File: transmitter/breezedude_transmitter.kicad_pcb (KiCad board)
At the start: 2 copper layers, 53 x 22.5 mm, 53 parts, among them J1 Conn_01x02_Pin, J11 Conn_01x04_Pin, J2 Conn_01x04_Pin, J3 Conn_01x04_Pin, J4 Conn_01x03_Pin, J5 Conn_01x04_Pin, J6 Conn_01x02_Pin, J7 USB_C_Receptacle_USB2.0_16P, Q2 P-MOS, Q3 P-MOS, SW1 SW_Push, U1 D1213A-04TS-7, U10 D1213A-04TS-7, U2 STLQ015M33R, U3 ATSAMD21G18A-A, U8 HP203B, U9 TP4057

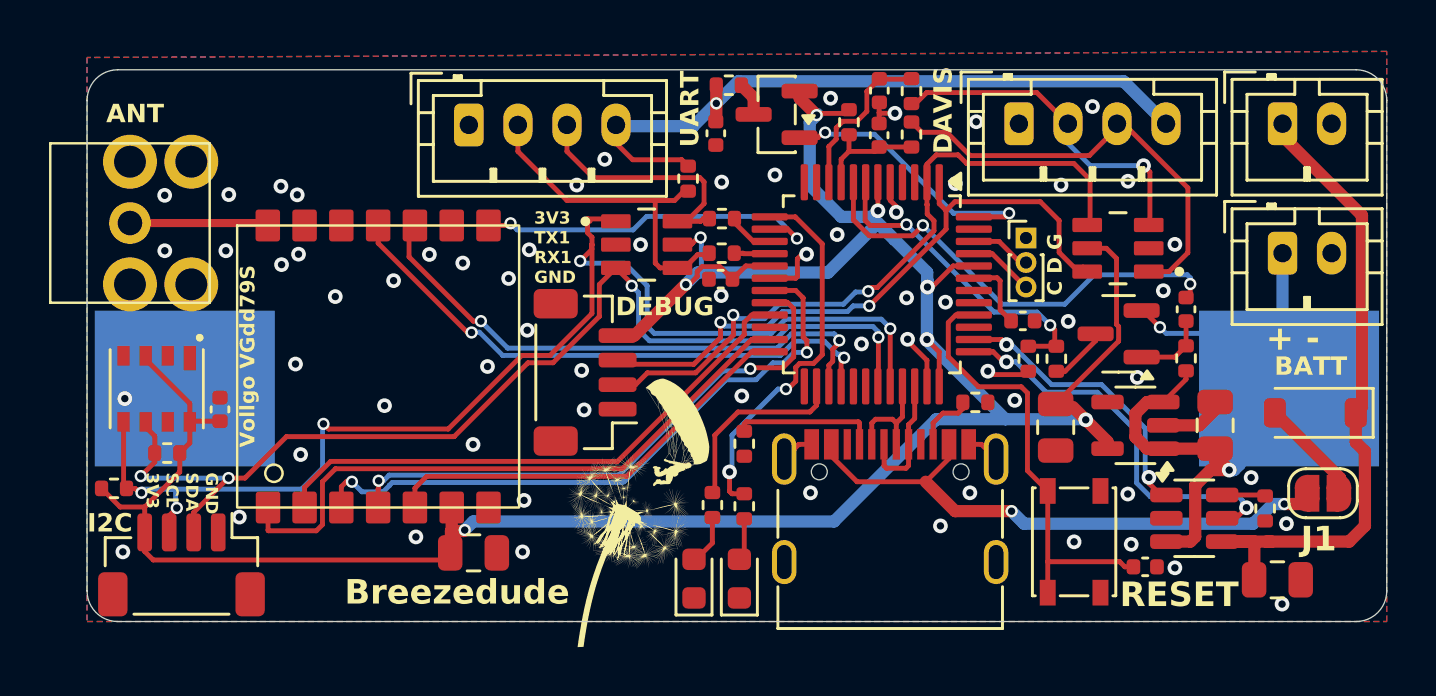
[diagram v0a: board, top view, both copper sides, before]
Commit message: V2.5 - some pin changes and improvements. Requires FW 1.2.0+
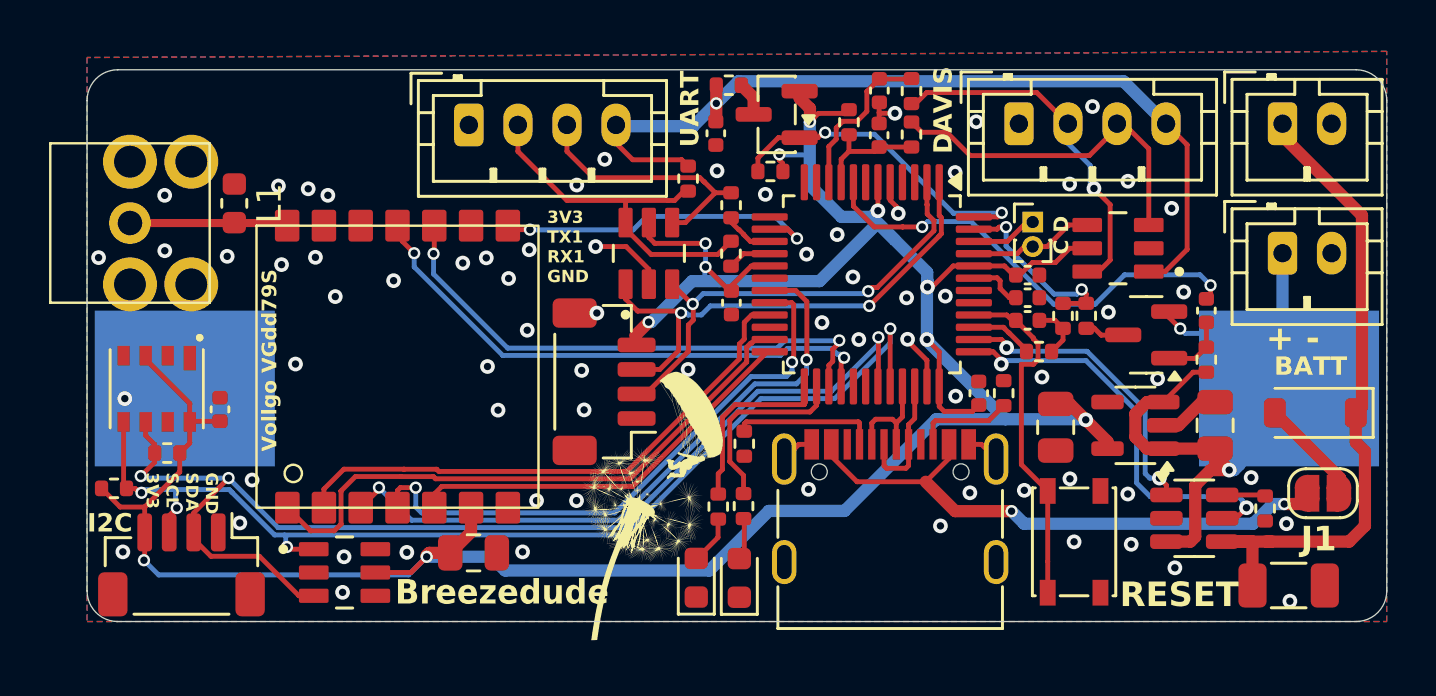
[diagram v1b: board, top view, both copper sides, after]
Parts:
- removed J4: Conn_01x03_Pin, Connector_PinHeader_1.00mm:PinHeader_1x03_P1.00mm_Vertical
- added C10: 100n 16V, Capacitor_SMD:C_0402_1005Metric, F.Cu at (133.4, 114.7)
- added C14: 100n 16V, Capacitor_SMD:C_0402_1005Metric, F.Cu at (135.4, 109.9)
- added J8: Conn_01x02_Pin, Connector_PinHeader_1.00mm:PinHeader_1x02_P1.00mm_Vertical, F.Cu at (135.6, 107.7)
- added L1: 68nH, Inductor_SMD:L_0603_1608Metric, F.Cu at (103.0, 106.9)
- added R18: 1M5, Resistor_SMD:R_0402_1005Metric, F.Cu at (124.9, 105.6)
- added R19: 4k7, Resistor_SMD:R_0402_1005Metric, F.Cu at (135.8, 113.0)
- added U11: D1213A-04TS-7, footprints:SOT95P280X140-6N, F.Cu at (119.9, 109.0)
- C1: value 47u 6.3V -> 47u 10V; footprint Capacitor_SMD:C_0805_2012Metric -> Capacitor_SMD:C_1206_3216Metric
- R13: value 4.7k -> 4k7
- moved U10 18.2 mm to (107.5, 122.0)
- moved C11 11.1 mm to (135.4, 111.7)
- moved R5 2.25 mm to (136.8, 111.5)
- moved R4 2.13 mm to (137.7, 111.5)
- moved D3 1.85 mm to (123.6, 122.2)
- moved D4 1.76 mm to (121.8, 122.2)
- moved R6 1.27 mm to (123.8, 119.3)
- moved R11 1.22 mm to (134.4, 114.7), turned to 90 degrees
- moved Q2 1.13 mm to (140.2, 112.3)
- moved R7 1.06 mm to (122.7, 119.3)
- moved C6 1.05 mm to (123.3, 111.0), turned to 90 degrees
- moved C2 0.96 mm to (135.4, 110.8)
- moved J11 0.86 mm to (118.1, 114.2)
- moved C9 0.83 mm to (142.6, 111.3)
- moved R3 0.83 mm to (142.6, 113.3)
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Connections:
- U1 pad 1: /DAVIS_SPEED -> /VCC_SENSOR
- U1 pad 3: /DAVIS_DIR -> /DAVIS_SPEED
- U1 pad 4: /RX1 -> /SWDCLK
- U1 pad 6: /TX1 -> /DAVIS_DIR
- U10 pad 4: /RX -> unconnected-(U10-IO3-Pad4)
- U10 pad 6: /TX -> unconnected-(U10-IO4-Pad6)
- U3 pad 13: /LED2 -> /LED2(alt)
- U3 pad 25: /LORA_DIO0 -> /LED2
- U3 pad 39: unconnected-(U3-PA27-Pad39) -> /HW_Ver1
- U3 pad 41: unconnected-(U3-PA28-Pad41) -> /HW_Ver2
- U3 pad 47: /EN_DCDC -> /V_DIV
- U3 pad 7: /V_DIV -> /V_DIV(alt)
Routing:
- net /RX1: track 28.0 -> 19.2 mm
- net 3V3: track 112.4 -> 120.4 mm, vias 8 -> 11
- net /LED2: track 15.5 -> 7.50 mm, vias 2 -> 0
- net /SCL: track 52.1 -> 44.6 mm, vias 5 -> 4
- net /VCC_SENSOR: track 29.5 -> 36.9 mm
- net /TX1: track 26.5 -> 20.9 mm
- net /V_DIV: track 13.1 -> 7.68 mm
- net /RESET: track 18.5 -> 14.3 mm
- net /DAVIS_SPEED: track 18.1 -> 14.3 mm
- net /SDA: track 44.6 -> 47.9 mm, vias 4 -> 3
- net /HW_Ver1: track 0.00 -> 2.59 mm
- net /SWDCLK: track 2.86 -> 5.11 mm
- net /SW_SENSOR: track 11.5 -> 13.5 mm
- net Net-(J7-CC2): track 2.58 -> 4.04 mm
- net GND: track 14.8 -> 16.1 mm, vias 65 -> 71
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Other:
- board text added: "C D"
- board text added: "CLK DIO"
- board text added: "V2.5"
- board text removed: "ANT"
- board text removed: "C D G"
- board text removed: "CLK DIO GND"
- board text removed: "DEBUG"
- board text removed: "V2.4"
